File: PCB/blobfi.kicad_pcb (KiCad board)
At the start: 2 copper layers, 52.5 x 64.8 mm, 14 parts, among them SW1 SW_Push, SW2 SW_Push, SW3 SW_Push, U1 XIAO-ESP32-C6-DIP, U2 HS96L03W2C03

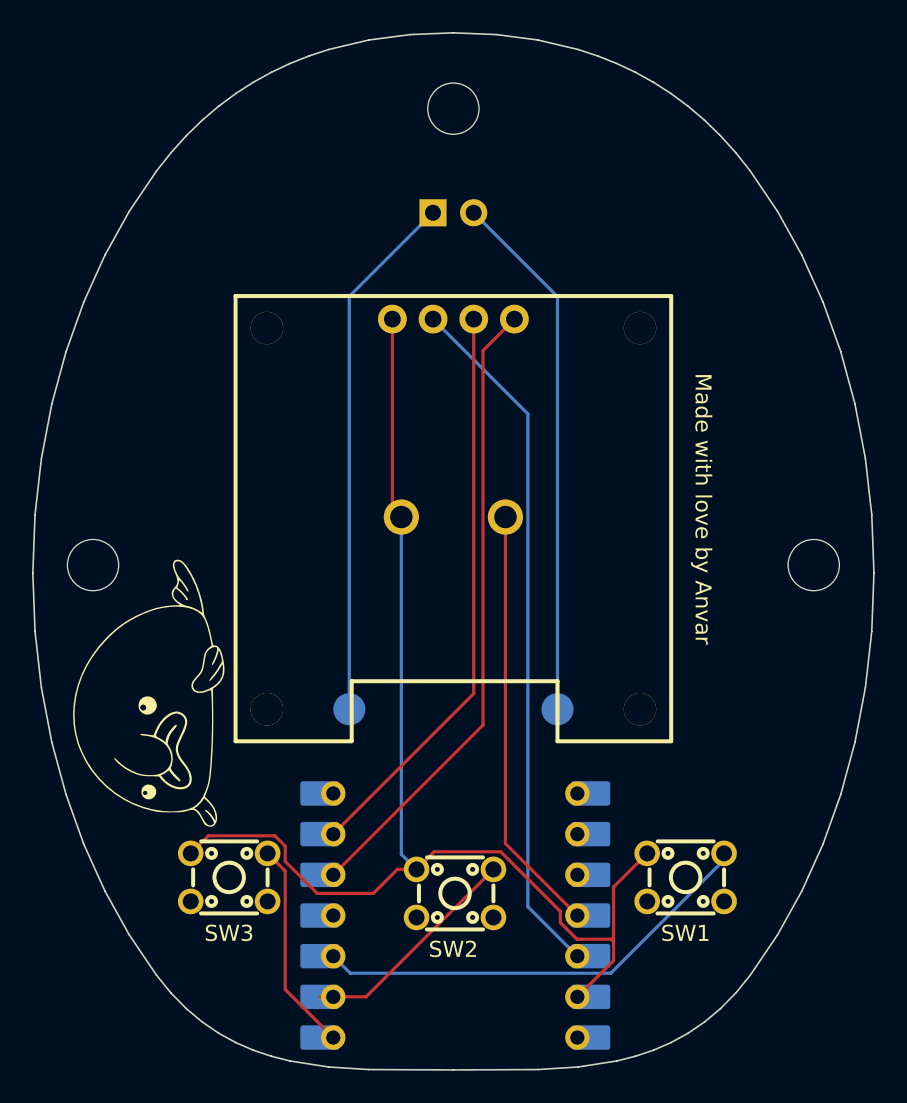
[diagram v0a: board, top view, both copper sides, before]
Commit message: add proper warning
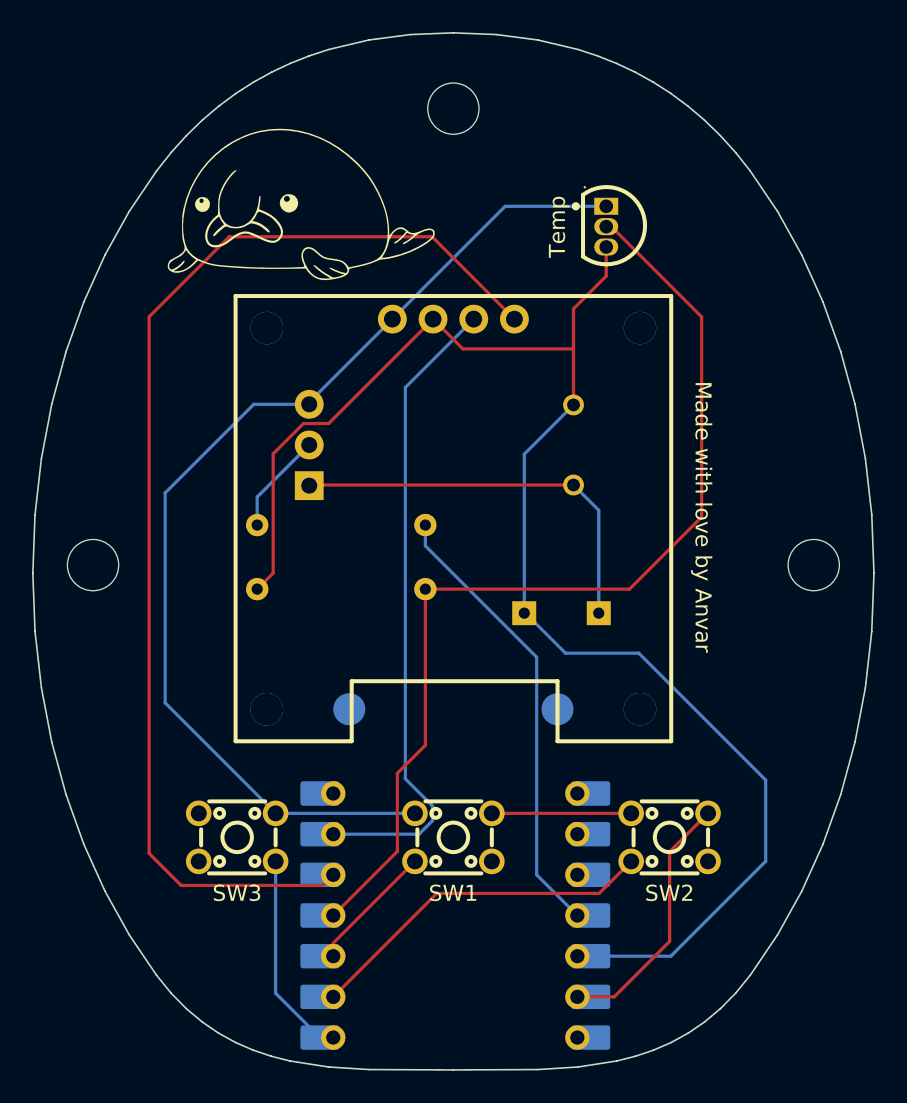
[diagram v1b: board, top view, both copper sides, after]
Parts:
- removed BT1: Battery_Cell, Connector_PinHeader_2.54mm:PinHeader_1x02_P2.54mm_Vertical
- removed BUZZER1: 1207-P6.5MM, easyeda2kicad:BUZ-TH_BD12.5-P6.50-D1.4
- removed the G*** at (165.0, 77.0)
- added C1: 100nF, easyeda2kicad:CAP-TH_L5.8-W3.6-P5.0-D0.6, B.Cu at (157.5, 78.0)
- added GND: Motor GND, TestPoint:TestPoint_THTPad_1.5x1.5mm_Drill0.7mm, B.Cu at (159.1, 88.5)
- added Q1: 2N2222A, easyeda2kicad:TO-92-3_L4.8-W3.7-P2.54-R, B.Cu at (141.0, 78.0)
- added R1: 4.7KΩ, easyeda2kicad:RES-TH_BD2.3-L6.5-P10.50-D0.5, B.Cu at (143.0, 87.0)
- added R2: 4.7KΩ, easyeda2kicad:RES-TH_BD2.3-L6.5-P10.50-D0.5, B.Cu at (143.0, 83.0)
- added Temp: MY18B20L, easyeda2kicad:TO-92-3_L4.8-W3.7-P1.27-L, F.Cu at (159.5, 64.4)
- added VCC: Motor VCC, TestPoint:TestPoint_THTPad_1.5x1.5mm_Drill0.7mm, B.Cu at (154.4, 88.5)
- moved G*** 31.9 mm to (140.5, 63.0), turned to 0 degrees
- moved SW1 14.7 mm to (150.0, 102.5)
- moved SW2 13.8 mm to (163.5, 102.5)
- moved SW3 2.55 mm to (136.5, 102.5)
- renumbered VBAT to TP1, GND to TP2
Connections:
- U1 pad 4: unconnected-(U1-GPIO21_D3-Pad4) -> Net-(U1-GPIO21_D3)
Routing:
- net Net-(U1-GPIO21_D3): track 0.00 -> 63.9 mm
- net +3V3: track 43.5 -> 95.5 mm
- net Net-(U1-GPIO22_D4_SDA): track 39.4 -> 73.1 mm
- net Net-(BT1--): track 33.2 -> 0.00 mm
- net Net-(BT1-+): track 33.2 -> 0.00 mm
- net Net-(Q1-C): track 0.00 -> 25.2 mm
- net Net-(U1-GPIO2_A2_D2): track 28.2 -> 8.03 mm
- net GND: track 78.5 -> 91.5 mm
- net Net-(U1-GPIO1_A1_D1): track 14.1 -> 22.1 mm
- net Net-(Q1-B): track 0.00 -> 6.35 mm
- net Net-(U1-GPIO23_D5_SCL): track 35.8 -> 40.3 mm
- net Net-(U1-GPIO18_D10_MOSI): track 26.7 -> 28.3 mm
- net Net-(U1-GPIO0_A0_D0): track 13.2 -> 12.1 mm
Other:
- board text added: "0.1uF"
- board text added: "4K7"
- board text added: "Motor"
- board text removed: "+"
- board text removed: "-"
